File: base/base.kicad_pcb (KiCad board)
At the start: 4 copper layers, 30 x 90 mm, 6 parts, among them J1 DF40TC(4.0)-30DS-0.4V(51), J2 DIP-48_SocketStrip_SMD

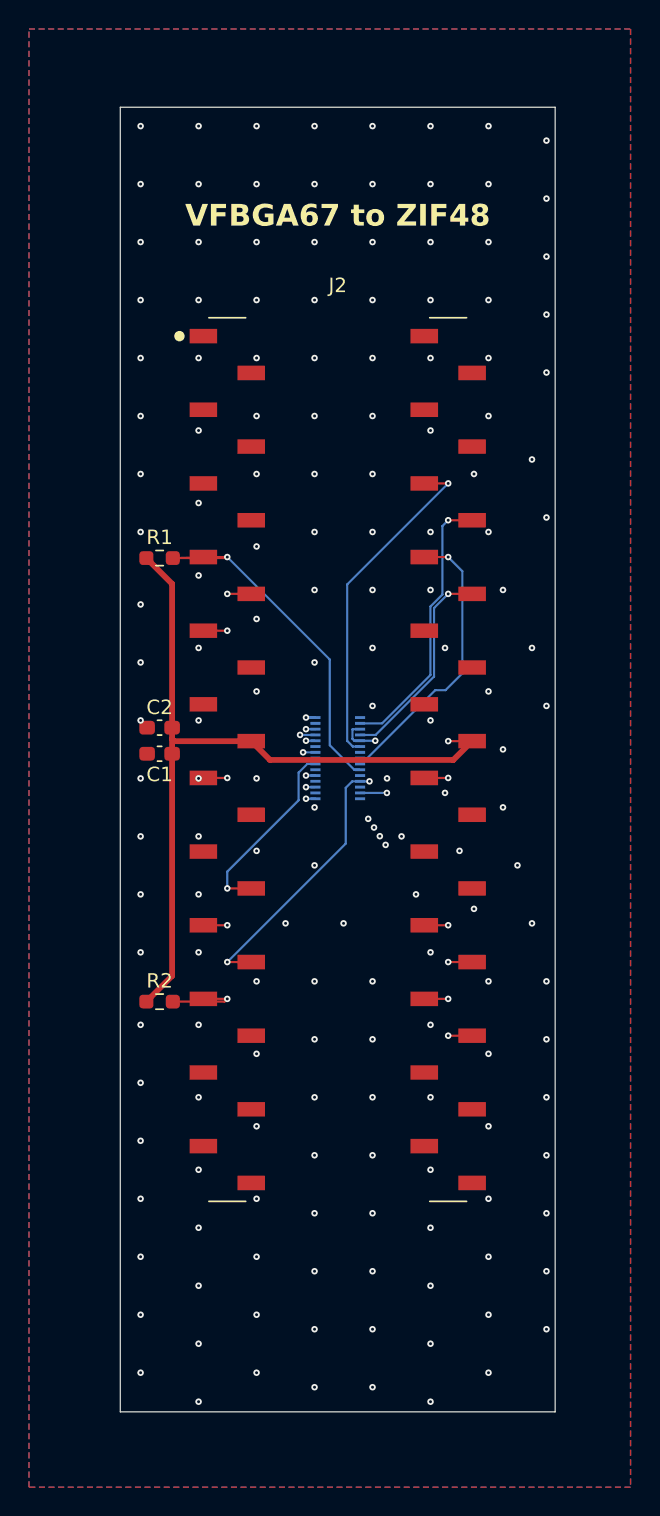
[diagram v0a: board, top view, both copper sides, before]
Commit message: Snapshot Courk-style unrouted NAND interposer
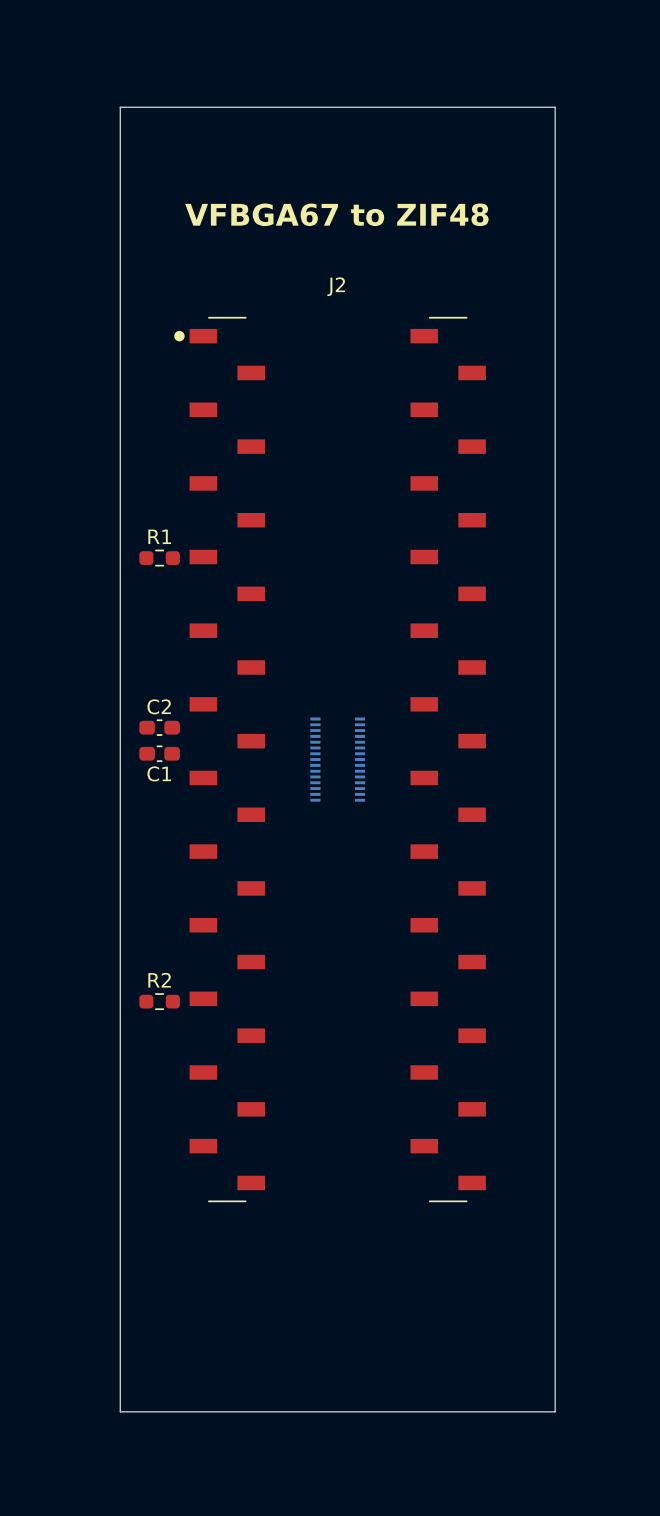
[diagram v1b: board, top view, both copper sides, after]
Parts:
- moved J1 0.10 mm to (124.1, 91.2)
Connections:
- J1 pad 1: /IO4 -> GND
- J1 pad 10: VCC -> //WP
- J1 pad 11: GND -> //CE
- J1 pad 12: /IO8 -> //RE
- J1 pad 13: /IO1 -> /CLE
- J1 pad 14: GND -> VCC
- J1 pad 16: /IO6 -> GND
- J1 pad 17: /CLE -> GND
- J1 pad 18: GND -> /IO5
- J1 pad 20: /RY//BY -> /IO2
- J1 pad 21: //RE -> /IO6
- J1 pad 22: GND -> /IO1
- J1 pad 23: GND -> /IO8
- J1 pad 24: //WE -> /IO3
- J1 pad 25: /ALE -> /IO7
- J1 pad 26: GND -> /IO4
- J1 pad 28: //CE -> GND
- J1 pad 29: //WP -> GND
- J1 pad 4: /IO7 -> GND
- J1 pad 5: /IO3 -> GND
- J1 pad 6: VCC -> GND
- J1 pad 7: GND -> /RY//BY
- J1 pad 8: /IO5 -> /ALE
- J1 pad 9: /IO2 -> //WE
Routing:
- net VCC: track 63.4 -> 0.00 mm, vias 2 -> 0
- net //WE: track 35.4 -> 0.00 mm, vias 2 -> 0
- net /RY//BY: track 27.9 -> 0.00 mm, vias 1 -> 0
- net /IO1: track 26.4 -> 0.00 mm, vias 2 -> 0
- net /IO2: track 24.2 -> 0.00 mm, vias 2 -> 0
- net /IO8: track 23.4 -> 0.00 mm, vias 1 -> 0
- net /IO3: track 22.4 -> 0.00 mm, vias 2 -> 0
- net //WP: track 22.2 -> 0.00 mm, vias 2 -> 0
- net /IO4: track 21.3 -> 0.00 mm, vias 2 -> 0
- net /IO6: track 19.6 -> 0.00 mm, vias 1 -> 0
- net //CE: track 19.3 -> 0.00 mm, vias 2 -> 0
- net /IO7: track 19.1 -> 0.00 mm, vias 1 -> 0
- net //RE: track 17.1 -> 0.00 mm, vias 2 -> 0
- net /IO5: track 14.5 -> 0.00 mm, vias 1 -> 0
- net /ALE: track 14.1 -> 0.00 mm, vias 2 -> 0
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- removed copper zone on B.Cu, net GND
- removed copper zone on F.Cu, net GND
- removed copper zone on In1.Cu, net GND
- removed copper zone on In2.Cu, net GND
